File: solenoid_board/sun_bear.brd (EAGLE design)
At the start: 38.1 x 38.1 mm, 32 parts, among them Q1 MOSFET-NCHANNELSMD, Q2 MOSFET-NCHANNELSMD, Q3 MOSFET-NCHANNELSMD, Q4 MOSFET-NCHANNELSMD

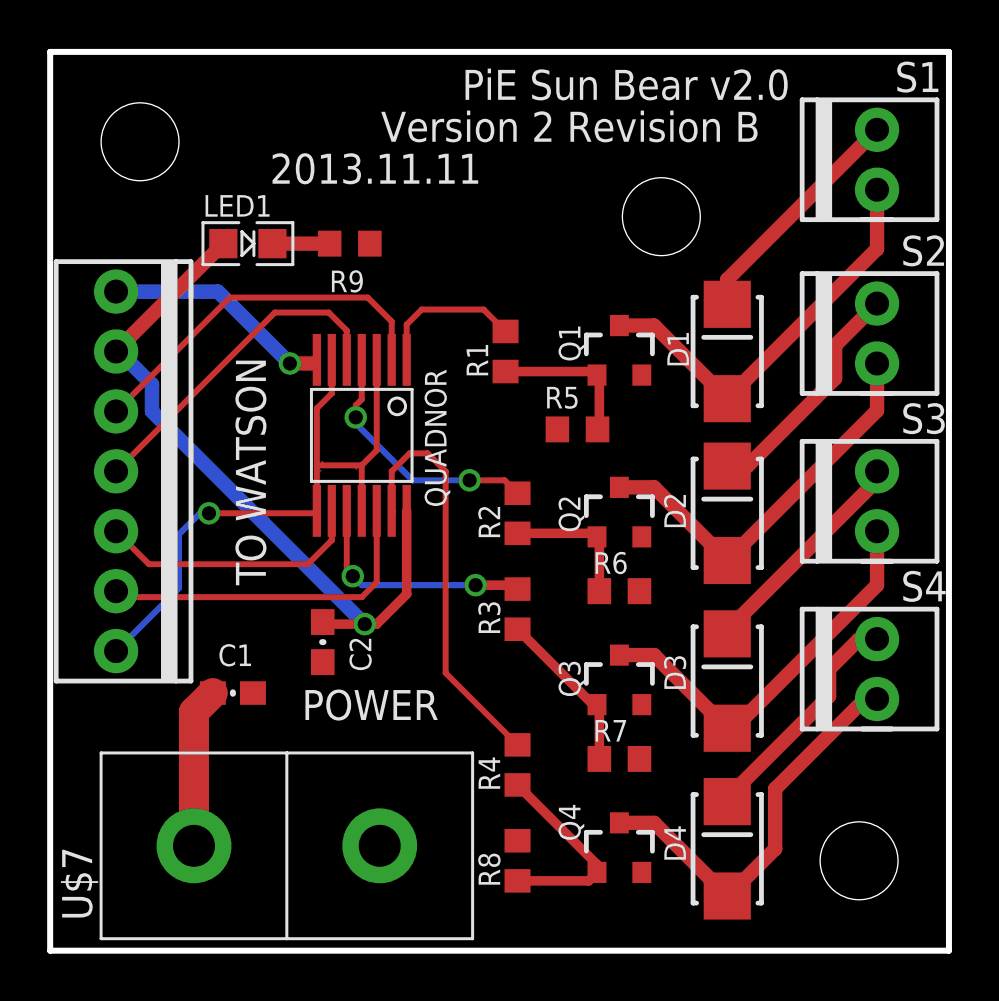
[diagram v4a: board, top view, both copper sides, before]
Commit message: Fixed schematics and added labels
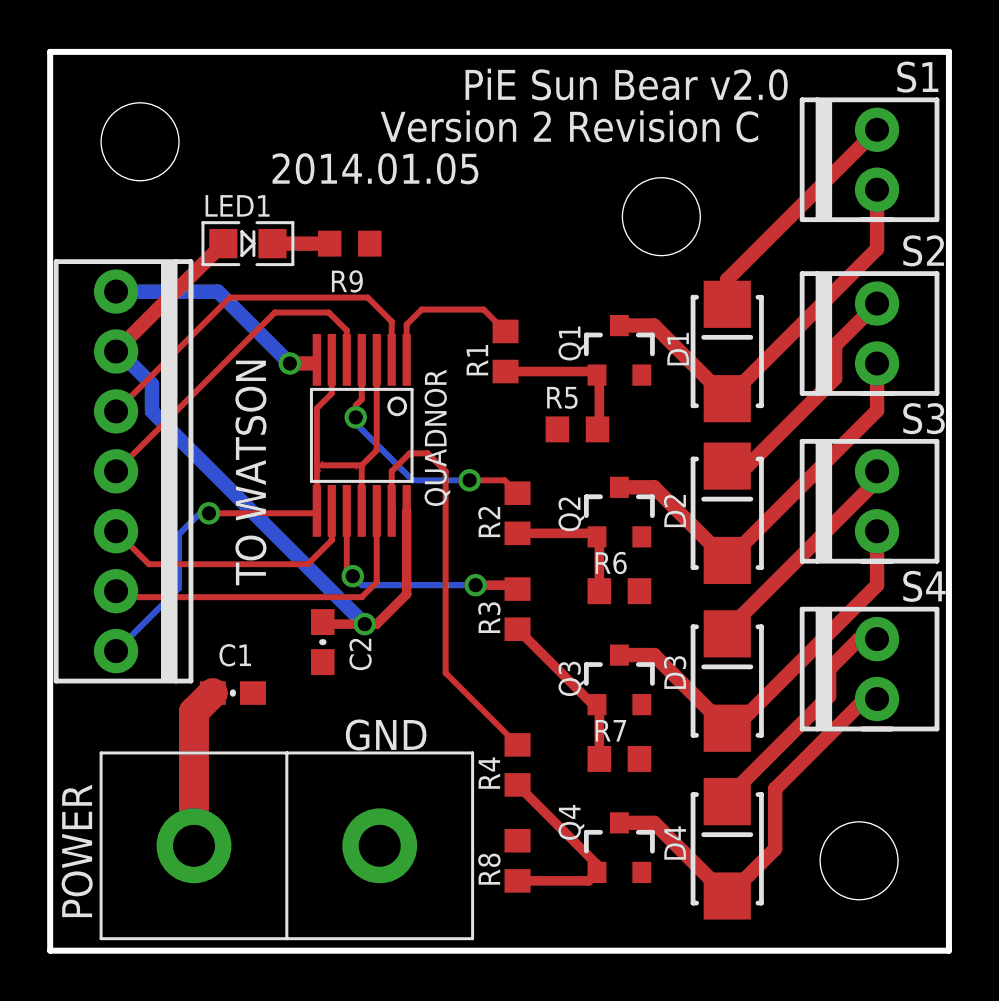
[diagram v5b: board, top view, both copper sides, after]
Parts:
- renumbered U$7 to POWER
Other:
- board text added: "2014.01.05"
- board text added: "GND"
- board text added: "Version 2 Revision C"
- board text removed: "2013.11.11"
- board text removed: "POWER"
- board text removed: "Version 2 Revision B"
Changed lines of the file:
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@@
 <wire x1="0" y1="38.1" x2="0" y2="0" width="0.254" layer="20"/>
 <text x="31.369" y="37.338" size="1.27" layer="25" font="vector" ratio="20" rot="R180">PiE Sun Bear v2.0</text>
-<text x="30.099" y="35.56" size="1.27" layer="21" font="vector" ratio="20" rot="R180">Version 2 Revision B</text>
-<text x="18.288" y="33.782" size="1.27" layer="21" font="vector" ratio="20" rot="R180">2013.11.11</text>
-<text x="10.668" y="9.779" size="1.27" layer="21" font="vector" ratio="20">POWER</text>
+<text x="30.099" y="35.56" size="1.27" layer="21" font="vector" ratio="20" rot="R180">Version 2 Revision C</text>
+<text x="18.288" y="33.782" size="1.27" layer="21" font="vector" ratio="20" rot="R180">2014.01.05</text>
+<text x="12.446" y="8.509" size="1.27" layer="21" font="vector">GND</text>
 <text x="9.144" y="15.494" size="1.27" layer="21" font="vector" ratio="20" rot="SR90">TO WATSON</text>
 <text x="33.655" y="8.89" size="1.27" layer="22" font="vector" ratio="15" rot="MR0">Copyright (c) 2013,
@@
 </element>
 <element name="U$6" library="pie" package="STAND-OFF" value="Mounting + Test" x="25.908" y="31.115"/>
-<element name="U$7" library="pie" package="ANDERSON_VERTICAL" value="ANDERSONVERTICAL" x="10.033" y="4.445" rot="R90">
+<element name="POWER" library="pie" package="ANDERSON_VERTICAL" value="ANDERSONVERTICAL" x="10.033" y="4.445" smashed="yes" rot="R90">
 <attribute name="PARTNUMBER" value="1377G3" x="10.033" y="4.445" size="1.778" layer="27" rot="R90" display="off"/>
+<attribute name="NAME" x="1.778" y="1.27" size="1.27" layer="25" font="vector" rot="R90"/>
 </element>
 </elements>
@@
 <wire x1="33.02" y1="11.938" x2="34.29" y2="13.208" width="0.6096" layer="1"/>
 <wire x1="34.29" y1="13.208" x2="35.052" y2="13.208" width="0.6096" layer="1"/>
-<contactref element="U$7" pad="PIN2"/>
+<contactref element="POWER" pad="PIN2"/>
 <wire x1="6.897" y1="10.922" x2="6.096" y2="10.121" width="1.27" layer="1"/>
 <wire x1="6.096" y1="10.121" x2="6.096" y2="4.445" width="1.27" layer="1"/>
@@
 <wire x1="2.794" y1="27.94" x2="7.112" y2="27.94" width="0.6096" layer="16"/>
 <wire x1="7.112" y1="27.94" x2="10.16" y2="24.892" width="0.6096" layer="16"/>
-<contactref element="U$7" pad="PIN1"/>
+<contactref element="POWER" pad="PIN1"/>
 </signal>
 <signal name="N$2">
